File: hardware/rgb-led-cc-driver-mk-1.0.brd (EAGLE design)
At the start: 46 x 40 mm, 18 parts, among them IC1 TINY85-20-DIP, J1 AVR_SPI_PRG_6PTH_INLINE_I2C, Q1 2N3904, Q2 IRLZ14PBF, Q3 2N3904, Q4 IRLZ14PBF, Q5 2N3904, Q6 IRLZ14PBF

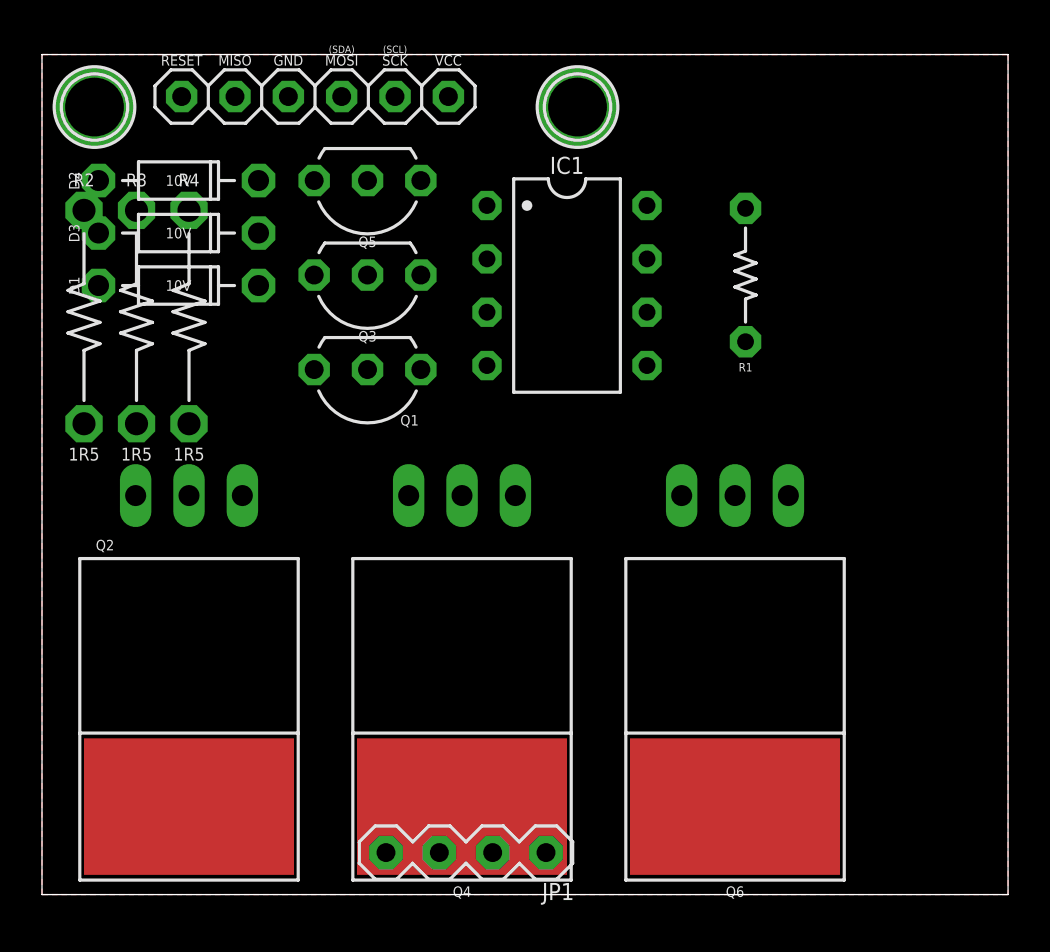
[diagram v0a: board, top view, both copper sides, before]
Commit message: layout for cc driver and some dicking around with the rgb one
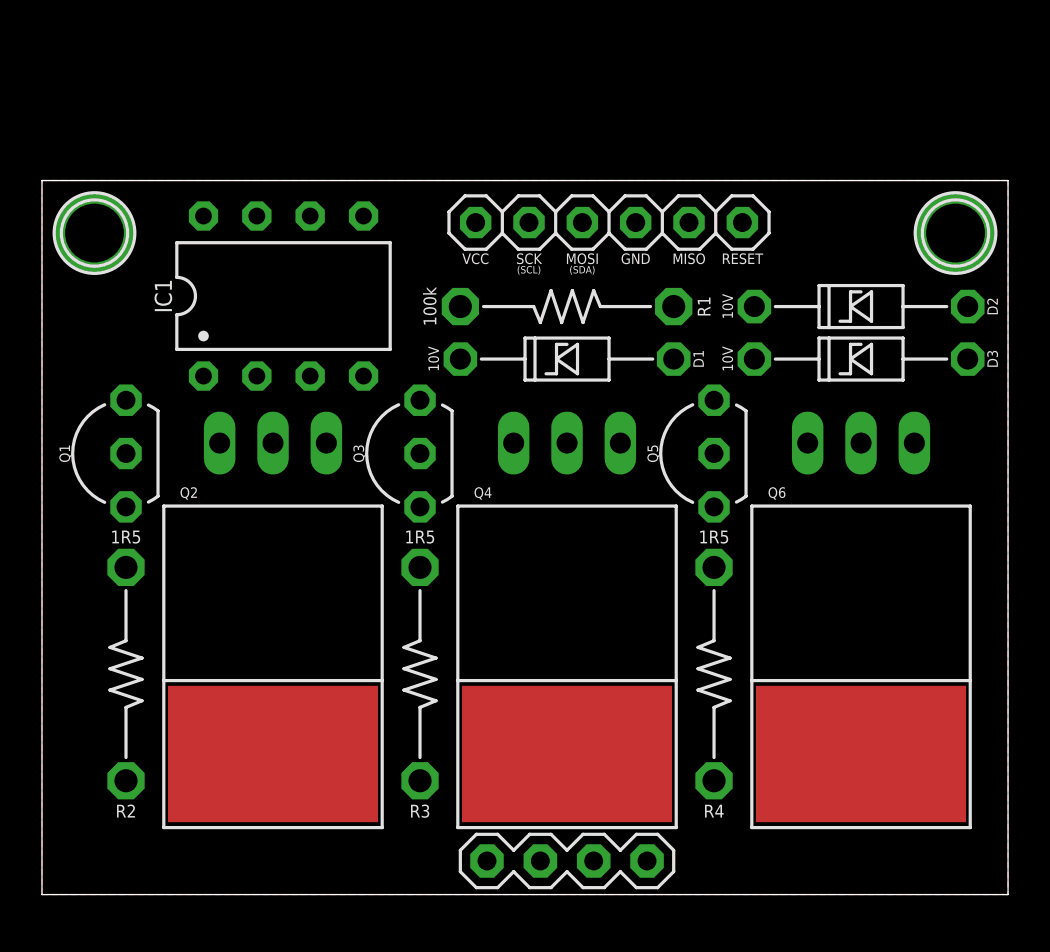
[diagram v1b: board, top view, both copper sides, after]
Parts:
- D1, D2, D3: device A_butts:DIODE-7.62MM -> A_butts:DIODE-ZENNER-10.16MM
- Q2, Q4, Q6: value IRLZ14PBF -> FQP30N06L
- R1: device A_butts:RESISTOR-AXIAL-PTH-6.35MM -> A_butts:RESISTOR-AXIAL-PTH-10.16MM
- moved D2 33.0 mm to (39.0, 28.0), turned to 180 degrees
- moved D3 33.0 mm to (39.0, 25.5), turned to 180 degrees
- moved R4 30.2 mm to (32.0, 10.5), turned to 90 degrees
- moved R3 21.7 mm to (18.0, 10.5), turned to 90 degrees
- moved Q5 21.0 mm to (32.0, 21.0), turned to 90 degrees
- moved H1 19.0 mm to (43.5, 31.5)
- moved D1 18.8 mm to (25.0, 25.5), turned to 180 degrees
- moved R2 17.1 mm to (4.00, 10.5), turned to 90 degrees
- moved J1 15.2 mm to (27.0, 32.0), turned to 0 degrees
- moved IC1 13.5 mm to (11.5, 28.5), turned to 0 degrees
- moved Q1 12.2 mm to (4.00, 21.0), turned to 90 degrees
- moved Q3 8.86 mm to (18.0, 21.0), turned to 90 degrees
- moved R1 8.63 mm to (25.0, 28.0), turned to 180 degrees
- moved Q6 6.50 mm to (39.0, 21.5)
- moved H2 6.00 mm to (2.50, 31.5)
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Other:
- board size 46 x 40 mm -> 46 x 34 mm
